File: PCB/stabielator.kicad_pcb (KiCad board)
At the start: 2 copper layers, 50 x 50 mm, 108 parts, among them J1 USB_C_Receptacle_USB2.0_16P, J2 Battery, J3 Motor 1, J4 Motor 2, J5 Motor 3, J6 Motor 4, Q1 2N7002, Q2 2N7002, SW1 PWR, SW2 BOOT, U1 DRV2605LDGS, U10 BQ24074RGT, U13 TLV62569DBV, U3 ESP32-C3-MINI-1, U4 TCA9546APW, U5 DRV2605LDGS, U6 DRV2605LDGS, U7 DRV2605LDGS, U8 USBLC6-2SC6, U9 TPS3424A11C13ADRLR

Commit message: Hopelijk definitief schema
Voornamelijk voeding opnieuw gemaakt;
Vervangen voor een buck boost systeem.
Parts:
- removed C16, C17, C18: 22uF, Capacitor_SMD:C_0805_2012Metric
- removed C38: 100nF, Capacitor_SMD:C_0603_1608Metric
- removed C44: 1uF, Capacitor_SMD:C_0805_2012Metric
- removed D6: LED_G, LED_SMD:LED_0603_1608Metric
- removed L1: 2.2uH, Inductor_SMD:L_1008_2520Metric
- removed Q1: 2N7002, Package_TO_SOT_SMD:SOT-23
- removed R50, R51, R52, R53, R54, R55, R56, R57: 4K7, Resistor_SMD:R_0603_1608Metric
- removed R66: 453K, Resistor_SMD:R_0603_1608Metric
- removed R67, R79: 100K, Resistor_SMD:R_0603_1608Metric
- removed R71, R72: 10K, Resistor_SMD:R_0603_1608Metric
- removed R75: 1K, Resistor_SMD:R_0603_1608Metric
- removed TP10: 3V3_DEBUG, TestPoint:TestPoint_Pad_D1.0mm
- removed TP14: VCC_DEBUG, TestPoint:TestPoint_Pad_D1.0mm
- removed TP3: CHIP_EN, TestPoint:TestPoint_Pad_D1.0mm
- removed U13: TLV62569DBV, Package_TO_SOT_SMD:SOT-23-5
- added C43: 10u, Capacitor_SMD:C_0805_2012Metric, F.Cu at (131.2, 56.6)
- added C46: 100n, Capacitor_SMD:C_0603_1608Metric, F.Cu at (132.6, 55.6)
- added C48: 10u, Capacitor_SMD:C_1206_3216Metric, F.Cu at (105.7, 83.5)
- added C50: 100n, Capacitor_SMD:C_0603_1608Metric, F.Cu at (106.8, 88.9)
- added C51: 10u, Capacitor_SMD:C_1206_3216Metric, F.Cu at (111.8, 89.5)
- added C52: 10u, Capacitor_SMD:C_1206_3216Metric, F.Cu at (110.1, 87.9)
- added L3: 2.2u, Inductor_SMD:L_Bourns-SRN4018, F.Cu at (111.1, 82.5)
- added R74: 100R, Resistor_SMD:R_0603_1608Metric, F.Cu at (104.7, 86.8)
- added TP15: VSYS_DEBUG, TestPoint:TestPoint_Pad_D1.0mm, F.Cu at (162.8, 96.2)
- added U40: TPS63001, Package_SON:Texas_DRC0010J_ThermalVias, F.Cu at (108.2, 85.4)
- C1: value 1n-2kV -> 1n
- C20, C24, C25, C26, C27, C29, C30, C31, C32: value 1uF -> 1u
- C21, C22, C23, C33, C34, C35, C36, C37, C41: value 100nF -> 100n
- C39, C40: value 4.7uF -> 4u7
- C42: value 1U -> 1u
- C45: value 4.7nF -> 4n7
- D5: value LED_R -> RED
- J1: value USB_C_Receptacle_USB2.0_16P -> USB4085-GF-A
- J2: value Battery -> S2B-PH
- J3: value Motor 1 -> SH_SM02B
- J4: value Motor 2 -> SH_SM02B
- J5: value Motor 3 -> SH_SM02B
- J6: value Motor 4 -> SH_SM02B
- R4, R73, R77: value 1K -> 1k
- R45, R48, R49, R58, R59, R60, R61, R63, R78: value 10K -> 10k
- R46, R47, R64, R65: value 4K7 -> 4k7
- R68: value 46.4K -> 46k4
- R69: value 1.13K -> 1k13
- R70: value 1.18K -> 1k18
- R76: value 100K -> 100k
- TP12: value IMU_BOOT -> 3V3_DEBUG
- U2: value ~ -> BNO086
- moved R45 24.6 mm to (132.9, 79.5), turned to -135 degrees
- moved R46 19.6 mm to (134.0, 80.5), turned to -135 degrees
- moved R47 19.3 mm to (135.0, 81.6), turned to -135 degrees
- moved C21 18.9 mm to (136.0, 82.6), turned to 45 degrees
- moved U4 16.7 mm to (131.3, 84.2), turned to -45 degrees
- moved R48 13.7 mm to (117.9, 55.6)
- moved C41 4.50 mm to (118.7, 88.4)
- moved U9 4.50 mm to (120.7, 88.4)
- moved R59 2.43 mm to (128.0, 59.5), turned to -90 degrees
- moved C45 1.90 mm to (117.0, 92.0)
- moved Q2 1.90 mm to (120.5, 92.2)
- moved R78 1.90 mm to (117.0, 93.5)
- moved C42 1.68 mm to (130.2, 58.0)
- moved R26 0.83 mm to (134.9, 75.4)
- moved R27 0.83 mm to (136.4, 75.4)
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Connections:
- net /CHIP_EN renamed /Logic/CHIP_EN
- C20 pad 1: GND -> 5V
- C20 pad 2: 5V -> GND
- C21 pad 1: GND -> 3V3
- C21 pad 2: +3.3V -> GND
- C22 pad 1: VCC -> 3V3
- C23 pad 1: VCC -> 3V3
- C25 pad 1: VCC -> 3V3
- C26 pad 1: VCC -> 3V3
- C30 pad 1: VCC -> 3V3
- C32 pad 1: VCC -> 3V3
- C33 pad 1: VCC -> 3V3
- C34 pad 1: VCC -> 3V3
- C36 pad 1: GND -> 3V3
- C36 pad 2: 3V3 -> GND
- C37 pad 1: GND -> 3V3
- C37 pad 2: 3V3 -> GND
- C39 pad 1: GND -> VSYS
- C39 pad 2: VCC -> GND
- C40 pad 1: GND -> VBAT
- C40 pad 2: +BATT -> GND
- C41 pad 1: VCC -> VSYS
- D5 pad 1: Net-(D5-K) -> (no net)
- D5 pad 2: VCC -> (no net)
- J1 pad A6: Net-(J1-D+-PadA6) -> Net-(J1-DP1)
- J1 pad A7: Net-(J1-D--PadA7) -> Net-(J1-DN1)
- J1 pad B6: Net-(J1-D+-PadA6) -> Net-(J1-DP1)
- J1 pad B7: Net-(J1-D--PadA7) -> Net-(J1-DN1)
- J2 pad 1: +BATT -> VBAT
- R26 pad 2: USB_D- -> USB_D+
- R27 pad 1: USB_D+ -> USB_D-
- R45 pad 1: +3.3V -> 3V3
- R46 pad 1: +3.3V -> 3V3
- R47 pad 1: +3.3V -> 3V3
- R58 pad 2: Net-(SW2-B) -> IO9_BOOT
- R63 pad 1: Net-(U2-~{BOOT}) -> 3V3
- R63 pad 2: 3V3 -> Net-(U2-~{BOOT})
- R73 pad 1: Net-(D5-K) -> VSYS
- R73 pad 2: Net-(Q1-G) -> Net-(D5-PadA)
- R76 pad 1: GND -> Net-(Q2-G)
- R76 pad 2: Net-(Q2-G) -> GND
- R78 pad 1: VCC -> VSYS
- SW1 pad 1: GND -> Net-(SW1-A)
- SW1 pad 2: Net-(SW1-B) -> GND
- SW2 pad 1: GND -> IO9_BOOT
- SW2 pad 2: Net-(SW2-B) -> GND
- TP1 pad 1: Net-(U3-GPIO21/U0TXD) -> Net-(U3-GPIO20/U0RXD)
- TP12 pad 1: Net-(U2-~{BOOT}) -> 3V3
- TP2 pad 1: Net-(U3-GPIO20/U0RXD) -> Net-(U3-GPIO21/U0TXD)
- U1 pad 10: VCC -> 3V3
- U1 pad 5: POWERSTATE -> 3V3
- U1 pad 6: unconnected-(U1-VDD/NC-Pad6) -> 3V3
- U10 pad 1: Net-(U10-TS) -> unconnected-(U10-TS-Pad1)
- U10 pad 10: VCC -> VSYS
- U10 pad 11: VCC -> VSYS
- U10 pad 2: +BATT -> VBAT
- U10 pad 3: +BATT -> VBAT
- U10 pad 9: Net-(Q1-G) -> CHG
- U3 pad 16: CHARGE -> unconnected-(U3-GPIO10-Pad16)
- U3 pad 23: Net-(SW2-B) -> IO9_BOOT
- U4 pad 16: +3.3V -> 3V3
- U5 pad 10: VCC -> 3V3
- U5 pad 5: POWERSTATE -> 3V3
- U5 pad 6: unconnected-(U5-VDD/NC-Pad6) -> 3V3
- U6 pad 10: VCC -> 3V3
- U6 pad 5: POWERSTATE -> 3V3
- U6 pad 6: unconnected-(U6-VDD/NC-Pad6) -> 3V3
- U7 pad 10: VCC -> 3V3
- U7 pad 5: POWERSTATE -> 3V3
- U7 pad 6: unconnected-(U7-VDD/NC-Pad6) -> 3V3
- U8 pad 1: Net-(J1-D--PadA7) -> Net-(J1-DP1)
- U8 pad 3: Net-(J1-D+-PadA6) -> Net-(J1-DN1)
- U9 pad 1: Net-(SW1-B) -> Net-(SW1-A)
- U9 pad 3: VCC -> VSYS
- U9 pad 6: POWERSTATE -> 3V3_EN
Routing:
- net Net-(U1-SDA): track 3.88 -> 0.00 mm
- net Net-(U1-SCL): track 4.53 -> 0.74 mm
- net Net-(U4-~{RESET}): track 3.24 -> 0.00 mm
- net Net-(U4-SC2): track 3.17 -> 0.00 mm
- net Net-(U4-SC1): track 3.08 -> 0.00 mm
- net Net-(U4-SD0): track 2.82 -> 0.00 mm
- net Net-(U4-SD1): track 2.75 -> 0.00 mm
- net Net-(U4-SD2): track 2.72 -> 0.00 mm
- net Net-(U4-SC0): track 2.49 -> 0.00 mm

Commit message: Reannotated schematic based on component placement
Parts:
- added C10: 100n, Capacitor_SMD:C_0603_1608Metric, F.Cu at (128.6, 64.0)
- added R1: 100k 0.1%, Resistor_SMD:R_0603_1608Metric, F.Cu at (117.4, 57.1)
- added R19: 10k, Resistor_SMD:R_0603_1608Metric, F.Cu at (115.6, 75.7)
- added R2: 300k 0.1%, Resistor_SMD:R_0603_1608Metric, F.Cu at (118.9, 57.1)
- added R23: 10k, Resistor_SMD:R_0603_1608Metric, F.Cu at (122.6, 80.0)
- J5: renamed from J1; value USB4085-GF-A -> USB4105-GF-A
- moved C7 28.7 mm to (117.0, 61.2), turned to 0 degrees
- moved R7 28.0 mm to (142.7, 68.6), turned to 45 degrees
- moved C11 27.2 mm to (120.1, 65.2), turned to 90 degrees
- moved C9 25.3 mm to (117.0, 63.5), turned to 0 degrees
- moved R4 24.2 mm to (120.1, 68.1), turned to 90 degrees
- moved U4 20.6 mm to (116.7, 66.7), turned to 0 degrees
- moved C14 17.7 mm to (117.0, 69.8), turned to 0 degrees
- moved L1 15.8 mm to (112.5, 66.7), turned to 90 degrees
- moved R10 13.8 mm to (109.5, 70.5)
- moved U9 13.5 mm to (107.2, 88.6), turned to 135 degrees
- moved R21 13.3 mm to (115.6, 77.1)
- moved Q1 12.1 mm to (110.1, 86.1), turned to -135 degrees
- moved R17 12.0 mm to (115.6, 74.2)
- moved C12 10.1 mm to (107.4, 66.0), turned to 90 degrees
- moved C28 10.1 mm to (108.7, 90.1), turned to -135 degrees
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- renumbered C46 to C1, C50 to C11, C20 to C12, C39 to C13, C48 to C14, C37 to C15, C30 to C16, C29 to C17, C33 to C18, C36 to C19, C43 to C2, C22 to C20, C24 to C21, C25 to C22, C35 to C23, C21 to C24, C1 to C25, C31 to C26, C45 to C27, C41 to C28, C34 to C29, C26 to C3, C32 to C30, C23 to C4, C42 to C5, C27 to C6, C51 to C7, C40 to C8, C52 to C9, D2 to D1, D5 to D2, H4 to H3, H3 to H4, J2 to J1, J4 to J2, J5 to J3, J3 to J4, L3 to L1, Q2 to Q1, R70 to R10, R60 to R11, R4 to R12, R49 to R13, R58 to R14, R26 to R15, R27 to R16, R68 to R17, R64 to R18, R65 to R20, R69 to R21, R63 to R22, R25 to R24, R47 to R25, R24 to R26, R46 to R27, R22 to R28, R45 to R29, R59 to R3, R78 to R30, R76 to R31, R77 to R32, R74 to R4, R73 to R5, R5 to R6, R48 to R7, R61 to R8, R3 to R9, SW2 to SW1, SW1 to SW2, TP15 to TP3, U3 to U1, U8 to U10, U1 to U11, U6 to U2, U10 to U3, U40 to U4, U7 to U5, U5 to U6, U2 to U7, U4 to U8
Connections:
- U1 pad 12: IMU_INT -> BATTERY
- U1 pad 16: unconnected-(U3-GPIO10-Pad16) -> IMU_INT
- U3 pad 1: unconnected-(U10-TS-Pad1) -> Net-(U10-TS)
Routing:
- net VSYS: track 0.00 -> 15.3 mm
- net SDA: track 3.34 -> 2.51 mm
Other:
- board text removed: "Power"

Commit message: Finish concept layout and routing
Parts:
- removed D2: RED, LED_SMD:LED_0603_1608Metric
- added D3: LED, LED_SMD:LED_0603_1608Metric, F.Cu at (101.3, 67.0)
- added IMG1: LOGO, LOGO, B.Cu at (145.8, 77.7)
- added TP14: EN_DEBUG, TestPoint:TestPoint_Pad_D1.0mm, B.Cu at (110.3, 89.2)
- added TP15: KILL_DEBUG, TestPoint:TestPoint_Pad_D1.0mm, B.Cu at (111.2, 81.6)
- added TP16: PSW_DEBUG, TestPoint:TestPoint_Pad_D1.0mm, B.Cu at (110.9, 97.4)
- added TP17: CHG_DEBUG, TestPoint:TestPoint_Pad_D1.0mm, B.Cu at (101.4, 64.0)
- added TP4: SCL_DEBUG, TestPoint:TestPoint_Pad_D1.0mm, B.Cu at (127.2, 81.9)
- added TP5: SDA_DEBUG, TestPoint:TestPoint_Pad_D1.0mm, B.Cu at (130.4, 79.8)
- added TP6: IMU_INT_DEBUG, TestPoint:TestPoint_Pad_D1.0mm, B.Cu at (125.1, 77.7)
- TP3: moved to B.Cu
- moved TP12 57.7 mm to (115.0, 57.3)
- moved TP3 47.3 mm to (115.7, 91.8), turned to 180 degrees
- moved TP11 33.9 mm to (132.9, 93.5)
- moved TP13 30.2 mm to (135.2, 93.5)
- moved TP1 29.9 mm to (139.4, 66.2), turned to -45 degrees
- moved TP2 29.0 mm to (140.9, 64.8), turned to -45 degrees
- moved R32 7.74 mm to (111.2, 85.4), turned to -90 degrees
- moved R31 6.93 mm to (112.8, 85.4), turned to 90 degrees
- moved C28 5.52 mm to (112.9, 93.6)
- moved U9 5.40 mm to (111.4, 92.1)
- moved R24 5.22 mm to (137.9, 80.3), turned to 180 degrees
- moved R30 5.09 mm to (108.6, 89.4), turned to -135 degrees
- moved R22 4.77 mm to (121.9, 82.0), turned to 90 degrees
- moved R28 4.72 mm to (137.9, 78.8), turned to 180 degrees
- moved R9 3.59 mm to (128.8, 67.8)
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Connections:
- C25 pad 1: Net-(C1-Pad1) -> Net-(J5-SHELL)
- J5 pad A6: Net-(J1-DP1) -> Net-(J5-DP1)
- J5 pad A7: Net-(J1-DN1) -> Net-(J5-DN1)
- J5 pad B6: Net-(J1-DP1) -> Net-(J5-DP1)
- J5 pad B7: Net-(J1-DN1) -> Net-(J5-DN1)
- J5 pad SH: (no net) -> Net-(J5-SHELL)
- R15 pad 2: USB_D+ -> USB_D-
- R16 pad 1: USB_D- -> USB_D+
- R26 pad 1: Net-(C1-Pad1) -> Net-(J5-SHELL)
- U10 pad 1: Net-(J1-DP1) -> Net-(J5-DN1)
- U10 pad 3: Net-(J1-DN1) -> Net-(J5-DP1)
- U7 pad 17: 3V3 -> GND
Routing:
- net 3V3: track 0.00 -> 188.5 mm, vias 0 -> 3
- net 5V: track 0.00 -> 74.0 mm, vias 0 -> 3
- net VSYS: track 15.3 -> 65.2 mm, vias 0 -> 1
- net 3V3_EN: track 0.00 -> 43.8 mm, vias 0 -> 2
- net IMU_RST: track 0.00 -> 42.3 mm, vias 0 -> 2
- net Net-(U2-SCL): track 0.00 -> 39.4 mm, vias 0 -> 2
- net Net-(U2-SDA): track 0.00 -> 37.7 mm, vias 0 -> 2
- net KILL: track 0.00 -> 37.2 mm, vias 0 -> 4
- net Net-(U5-SCL): track 0.00 -> 32.9 mm, vias 0 -> 2
- net Net-(U5-SDA): track 0.00 -> 32.2 mm, vias 0 -> 2
- net SCL: track 4.49 -> 32.2 mm, vias 0 -> 3
- net BATTERY: track 0.00 -> 25.0 mm, vias 0 -> 2
- net SDA: track 2.51 -> 26.8 mm, vias 0 -> 3
- net IMU_INT: track 0.00 -> 18.8 mm, vias 0 -> 2
- net Net-(U3-TMR): track 0.00 -> 17.9 mm, vias 0 -> 2
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- added copper zone on F.Cu, net 3V3
- added copper zone on F.Cu, net 5V
- added copper zone on In1.Cu, net GND
- added copper zone on In2.Cu, net GND
- added copper zone on F.Cu, net Net-(J5-SHELL)
- added copper zone on F.Cu, net VBAT
- added copper zone on F.Cu, net VSYS
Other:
- copper layers 2 -> 4
- board text added: "09-2026 v0.1"

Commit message: Geographical reannotation
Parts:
- removed IMG1: LOGO, LOGO
- moved TP10 0.64 mm to (115.8, 91.2)
- renumbered C16 to C14, C14 to C15, C17 to C16, C15 to C17, C20 to C19, C19 to C20, C27 to C26, C26 to C27, C29 to C28, C30 to C29, C28 to C30, C7 to C5, C5 to C6, C6 to C7, D3 to D2, R12 to R10, R8 to R11, R11 to R12, R19 to R15, R21 to R16, R18 to R17, R17 to R18, R20 to R19, R28 to R20, R24 to R21, R15 to R22, R25 to R23, R26 to R24, R31 to R25, R32 to R26, R16 to R27, R27 to R28, R22 to R29, R23 to R30, R29 to R31, R30 to R32, R6 to R4, R9 to R5, R4 to R6, R5 to R7, R7 to R8, R10 to R9, TP12 to TP1, TP3 to TP10, TP13 to TP11, TP11 to TP12, TP16 to TP13, TP17 to TP2, TP2 to TP3, TP1 to TP4, TP6 to TP5, TP5 to TP6, TP15 to TP7, TP4 to TP8, TP14 to TP9, U11 to U10, U9 to U11, U10 to U9
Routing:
- net 5V: track 74.0 -> 73.2 mm
- net GND: vias 155 -> 188

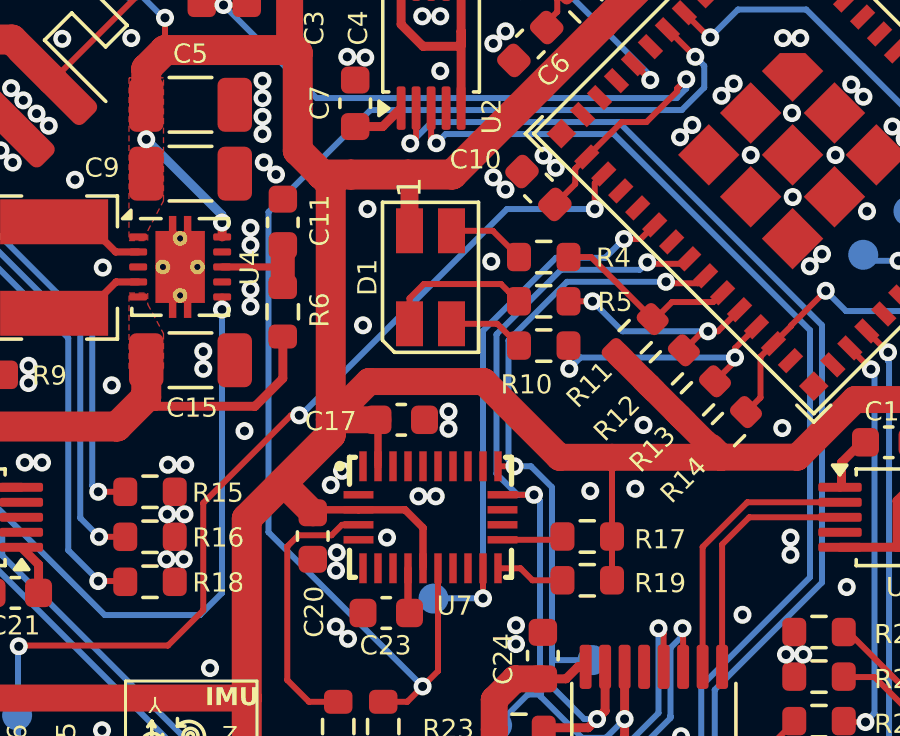
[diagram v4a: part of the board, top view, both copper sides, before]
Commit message: Activate thermal reliefs (excluding buck/charge)
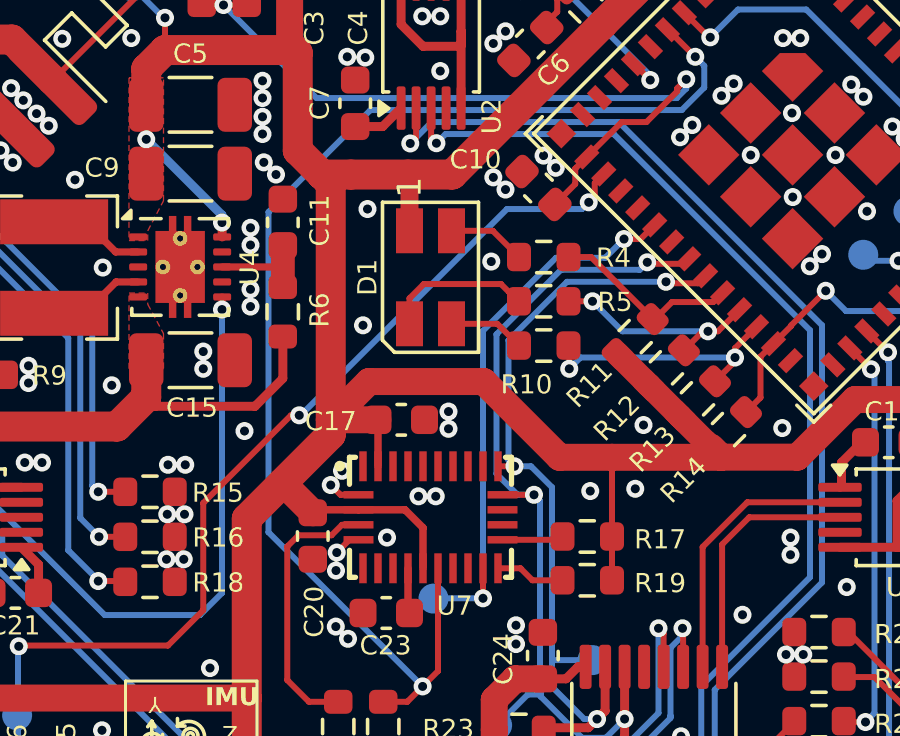
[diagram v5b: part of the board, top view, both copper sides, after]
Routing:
- net GND: track 2.51 -> 4.47 mm
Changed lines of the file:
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@@
 			)
 		)
+		(zone_connect 2)
 		(attr smd)
 		(duplicate_pad_numbers_are_jumpers no)
@@
 			(pinfunction "Pin_2_2")
 			(pintype "passive")
+			(zone_connect 2)
 		)
 		(pad "MP" smd roundrect
@@
 			(net "GND")
 			(pintype "passive")
+			(zone_connect 2)
 		)
 		(embedded_fonts no)
@@
 			)
 		)
+		(zone_connect 2)
 		(attr smd)
 		(duplicate_pad_numbers_are_jumpers no)
@@
 			(net "GND")
 			(pintype "passive")
+			(zone_connect 2)
 		)
 		(embedded_fonts no)
@@
 			)
 		)
+		(zone_connect 2)
 		(attr smd)
 		(duplicate_pad_numbers_are_jumpers no)
@@
 			(net "GND")
 			(pintype "passive")
+			(zone_connect 2)
 		)
 		(embedded_fonts no)
@@
 			(net "GND")
 			(pintype "passive")
+			(zone_connect 2)
 		)
 		(embedded_fonts no)
@@
 			)
 		)
+		(zone_connect 2)
 		(attr smd)
 		(duplicate_pad_numbers_are_jumpers no)
@@
 	)
 	(segment
+		(start 122.6 75.75)
+		(end 122.3 75.75)
+		(width 0.2)
+		(layer "F.Cu")
+		(net "GND")
+	)
+	(segment
+		(start 122.3 75.75)
+		(end 121.875 76.175)
+		(width 0.2)
+		(layer "F.Cu")
+		(net "GND")
+	)
+	(segment
+		(start 122 74.25)
+		(end 121.675 73.925)
+		(width 0.2)
+		(layer "F.Cu")
+		(net "GND")
+	)
+	(segment
 		(start 142.375 87.6)
 		(end 143.16967 88.39467)
@@
 	)
 	(segment
+		(start 122.6 74.25)
+		(end 122 74.25)
+		(width 0.2)
+		(layer "F.Cu")
+		(net "GND")
+	)
+	(segment
 		(start 138.644186 92.936747)
 		(end 138.163265 92.455826)
@@
 	)
 	(segment
+		(start 130.475 64.3)
+		(end 130.475 63.856774)
+		(width 0.2)
+		(layer "F.Cu")
+		(net "KILL")
+	)
+	(segment
+		(start 130.475 63.856774)
+		(end 130.776241 63.555533)
+		(width 0.2)
+		(layer "F.Cu")
+		(net "KILL")
+	)
+	(segment
 		(start 111.25 86.25)
 		(end 111.25 87.05)
@@
 	)
 	(segment
-		(start 130.475 64.725)
-		(end 130.475 63.856774)
-		(width 0.2)
-		(layer "F.Cu")
-		(net "KILL")
-	)
-	(segment
 		(start 117.425 78.1)
 		(end 117.425 74.525)
@@
 	)
 	(segment
-		(start 130.475 63.856774)
-		(end 130.776241 63.555533)
+		(start 130.275 64.5)
+		(end 130.475 64.3)
 		(width 0.2)
 		(layer "F.Cu")
@@
 	)
 	(via
-		(at 130.475 64.725)
+		(at 130.275 64.5)
 		(size 0.6)
 		(drill 0.3)
@@
 	(segment
 		(start 127.55 64.725)
-		(end 130.475 64.725)
+		(end 120.675 71.6)
 		(width 0.2)
 		(layer "B.Cu")
@@
 	)
 	(segment
-		(start 111.25 87.05)
-		(end 111.25 79.325)
+		(start 130.05 64.725)
+		(end 127.55 64.725)
+		(width 0.2)
+		(layer "B.Cu")
+		(net "KILL")
+	)
+	(segment
+		(start 130.275 64.5)
+		(end 130.05 64.725)
 		(width 0.2)
 		(layer "B.Cu")
@@
 	(segment
 		(start 120.675 71.6)
-		(end 127.55 64.725)
+		(end 120.625 71.6)
 		(width 0.2)
 		(layer "B.Cu")
@@
 	)
 	(segment
-		(start 120.625 71.6)
-		(end 120.675 71.6)
+		(start 111.25 87.05)
+		(end 111.25 79.325)
 		(width 0.2)
 		(layer "B.Cu")
@@
 		(layers "F.Cu" "B.Cu" "In1.Cu" "In2.Cu")
 		(hatch edge 0.5)
-		(connect_pads yes
+		(connect_pads
 			(clearance 0.2)
 		)
 		(min_thickness 0.2)
 		(fill yes
-			(thermal_gap 0.5)
+			(thermal_gap 0.2)
 			(thermal_bridge_width 0.5)
 			(island_removal_mode 0)

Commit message: change size of logic tab A4->A3 and create production files
Gerbers generated for JLCpcb, settings for other producer are unknown
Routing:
- net GND: track 4.47 -> 6.74 mm
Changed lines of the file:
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@@
+	)
+	(segment
+		(start 111.732107 92.782107)
+		(end 111.3 92.35)
+		(width 0.2)
+		(layer "F.Cu")
+		(net "GND")
 	)
 	(segment
@@
 		(start 122.6 75.75)
 		(end 122.3 75.75)
+		(width 0.2)
+		(layer "F.Cu")
+		(net "GND")
+	)
+	(segment
+		(start 111.742893 92.782107)
+		(end 111.732107 92.782107)
 		(width 0.2)
 		(layer "F.Cu")
@@
 		(width 0.2)
 		(layer "F.Cu")
+		(net "GND")
+	)
+	(segment
+		(start 112.378984 93.418198)
+		(end 112.378984 94.171016)
+		(width 0.2)
+		(layer "F.Cu")
+		(net "GND")
+	)
+	(segment
+		(start 111.742893 92.782107)
+		(end 112.378984 93.418198)
+		(width 0.2)
+		(layer "F.Cu")

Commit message: Ready for production
Small readability and producability optimizations
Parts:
- R1: value 100k 0.1% -> 100k
- R2: value 300k 0.1% -> 300k
- moved TP12 1.35 mm to (131.6, 93.4)
- moved R29 0.22 mm to (121.7, 82.0)
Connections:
- SW2 pad MP: (no net) -> GND
- U7 pad 1: (no net) -> unconnected-(U7-RESV_NC-Pad1)
- U7 pad 12: (no net) -> unconnected-(U7-RESV_NC-Pad12)
- U7 pad 13: (no net) -> unconnected-(U7-RESV_NC-Pad13)
- U7 pad 21: (no net) -> unconnected-(U7-RESV_NC-Pad21)
- U7 pad 22: (no net) -> unconnected-(U7-RESV_NC-Pad22)
- U7 pad 23: (no net) -> unconnected-(U7-RESV_NC-Pad23)
- U7 pad 24: (no net) -> unconnected-(U7-RESV_NC-Pad24)
- U7 pad 7: (no net) -> unconnected-(U7-RESV_NC-Pad7)
- U7 pad 8: (no net) -> unconnected-(U7-RESV_NC-Pad8)
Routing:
- net 3V3: track 188.5 -> 192.0 mm
- net USB_D-: track 14.3 -> 17.7 mm
- net Net-(R27-Pad2): track 3.60 -> 6.59 mm
- net USB_D+: track 16.3 -> 18.5 mm
- net Net-(R22-Pad1): track 6.40 -> 7.63 mm
- net Net-(U1-GPIO2/ADC1_CH2): track 17.7 -> 16.9 mm
- net 5V: track 73.2 -> 72.8 mm, vias 3 -> 5
- net GND: vias 188 -> 189
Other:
- rule pad_to_mask_clearance: 0 -> 0.05
- board text added: "${Project_name}"
- board text added: "${Project_name} ${Project_revision}"
- board text added: "${Project_revision}"
- board text removed: "09-2026 v0.1"
- board text removed: "Stabielator"
- board text removed: "V0.1"
